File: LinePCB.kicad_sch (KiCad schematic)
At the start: 205 parts, among them J1 Conn_01x12, U1 MCP3008, U2 MCP3008, U3 MCP3008, U4 MCP3008, U5 MCP3008, U6 MCP3008

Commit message: Placement
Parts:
- added D97: LED, LED_SMD:LED_0805_2012Metric_Pad1.15x1.40mm_HandSolder, symbol Device:LED
- added J3: Conn_01x03, Connector_JST:JST_XH_B3B-XH-A_1x03_P2.50mm_Vertical, symbol Connector_Generic:Conn_01x03
- added R103: 25, Package_TO_SOT_THT:TO-220-2_Vertical, symbol Device:R
- added U10: Optocoupler, Package_DIP:DIP-4_W7.62mm, symbol Isolator:NSL-32
- added U11, U14: 210, Resistor_SMD:R_0805_2012Metric_Pad1.20x1.40mm_HandSolder, symbol Device:R
- added U12, U13: 2200, Capacitor_THT:CP_Radial_D18.0mm_P7.50mm, symbol Line-PCB-rescue:CP1-Device
- added U15: Oprocoupler, Package_DIP:DIP-4_W7.62mm, symbol Isolator:NSL-32
- added U16: 10k, Resistor_SMD:R_0805_2012Metric_Pad1.20x1.40mm_HandSolder, symbol Device:R
- added U17: N channel, Package_TO_SOT_THT:TO-220-3_Vertical, symbol Transistor_FET:2N7002K
- added U18: D, Diode_THT:D_5W_P12.70mm_Horizontal, symbol Device:D
- added U19: 10K, Resistor_SMD:R_0805_2012Metric_Pad1.20x1.40mm_HandSolder, symbol Device:R
- added U20: Conn_01x02, SMDPads:Pads, symbol Connector_Generic:Conn_01x02
- added U7: 30k, Resistor_SMD:R_0805_2012Metric_Pad1.20x1.40mm_HandSolder, symbol Device:R
- added U8: 115k, Resistor_SMD:R_0805_2012Metric_Pad1.20x1.40mm_HandSolder, symbol Device:R
- added U9: BSP89, Package_TO_SOT_THT:TO-220-3_Vertical, symbol Transistor_FET:BSP89
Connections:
- net GND: now also D97.1 (K), J3.2 (Pin_2), U10.2 (K), U12.2, U13.2, U15.2 (K), U17.3 (D), U19.1, U8.1
- net 5V renamed Kicker
- net Kicker: now also U11.2, U14.1
- new net: U14.2, U15.1 (A)
- new net: U15.3 (R), U17.1 (G), U19.2
- new net: U17.2 (S), U18.2 (A), U20.2 (Pin_2)
- new net: R103.1, U12.1, U13.1, U16.2, U18.1 (K), U20.1 (Pin_1)
- new net: D97.2 (A), U16.1
- new net: U10.1 (A), U11.1
- new net: R103.2, U9.2 (D)
- new net: U10.3 (R), U7.1, U8.2, U9.1 (G)
- new net 12V: J3.3 (Pin_3), U15.4 (R)
- new net 48V: J3.1 (Pin_1), U10.4 (R), U7.2, U9.3 (S)
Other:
- moved on the sheet: J1

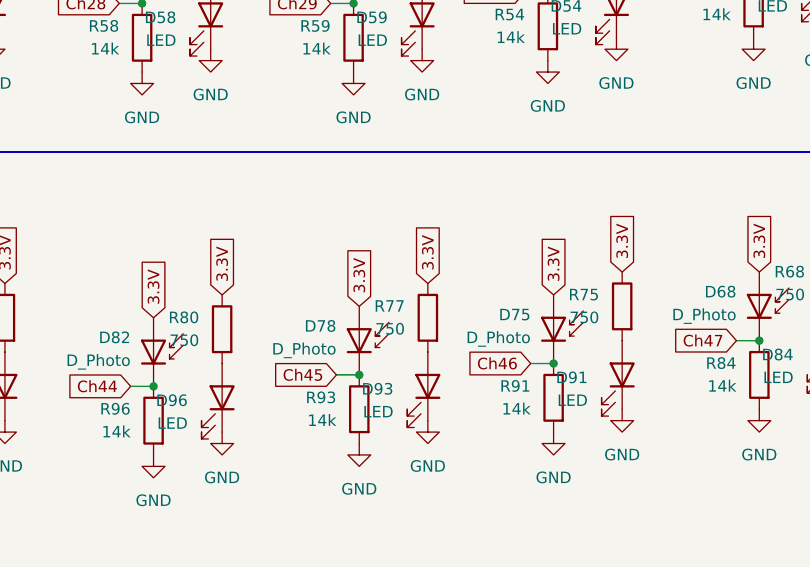
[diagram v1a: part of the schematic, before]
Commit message: Finished routing, needs clearing up clearance errors
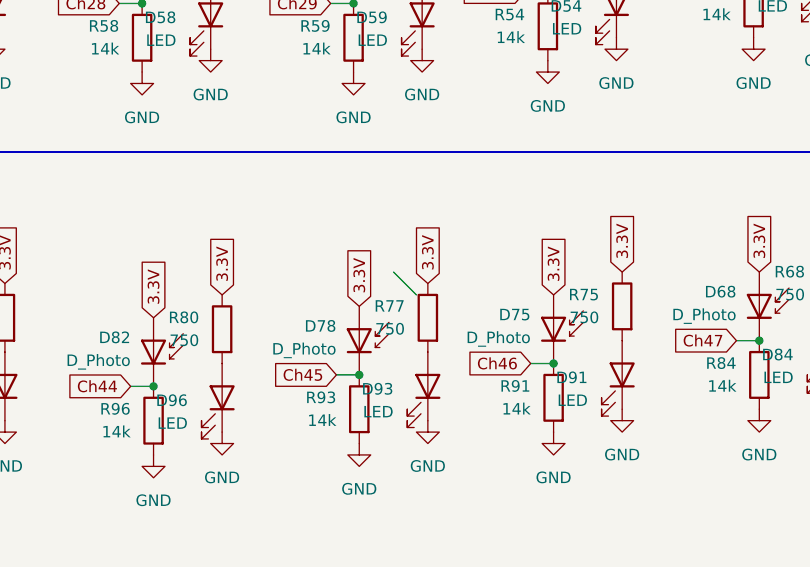
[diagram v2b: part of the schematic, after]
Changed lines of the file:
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@@
 		(color 0 0 0 0)
+	)
+	(bus_entry
+		(at 323.85 110.49)
+		(size 2.54 2.54)
+		(stroke
+			(width 0)
+			(type default)
+		)
 	)
 	(wire

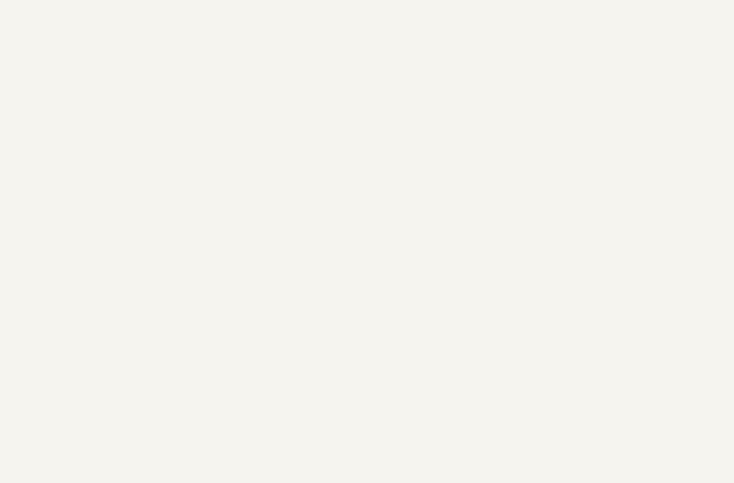
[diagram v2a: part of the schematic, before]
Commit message: added voltage reg
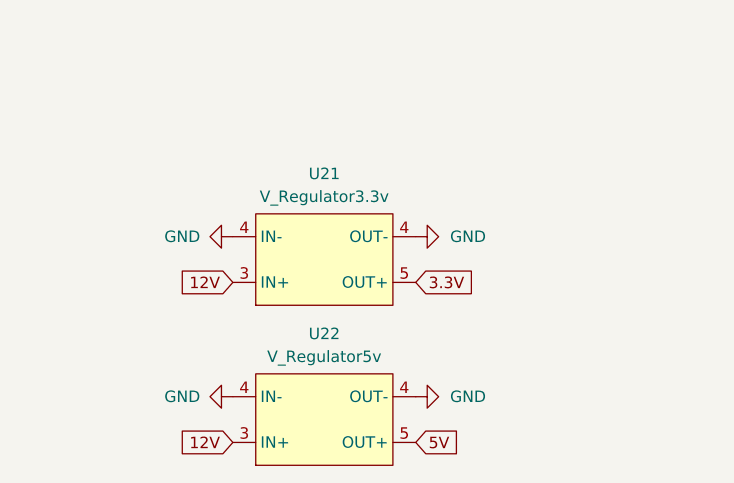
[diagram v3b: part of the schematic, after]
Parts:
- added U21: V_Regulator3.3v, Custom1:Pololu5V3.4A, symbol Voltage Regulator:V_Regulator_-_5v
- added U22: V_Regulator5v, Custom1:Pololu5V3.4A, symbol Voltage Regulator:V_Regulator_-_5v
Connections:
- net 12V: now also U21.3 (IN+), U22.3 (IN+)
- net 3.3V: now also U21.5 (OUT+)
- net GND: now also U21.4 (OUT-), U22.4 (OUT-)
- new net 5V: U22.5 (OUT+)

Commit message: Added JST
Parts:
- added J4: Conn_01x05_Pin, Connector_JST:JST_XH_B5B-XH-A_1x05_P2.50mm_Vertical, symbol Connector:Conn_01x05_Pin
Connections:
- net 12V: now also J4.1 (Pin_1)
- net 3.3V: now also J4.3 (Pin_3)
- net 48V: now also J4.5 (Pin_5)
- net 5V: now also J4.2 (Pin_2)
- net GND: now also J4.4 (Pin_4)
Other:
- moved on the sheet: J1, U21, U22
